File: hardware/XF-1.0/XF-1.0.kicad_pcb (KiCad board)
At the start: 2 copper layers, 121.3 x 99.7 mm, 16 parts

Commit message: modified:   Ferrite Transformer Calculation.xlsx 	modified:   README.md 	deleted:    hardware/XF-1.0/XF-1.0-backups/XF-1.0-2025-07-15_095716.zip 	new file:   hardware/XF-1.0/XF-1.0-backups/XF-1.0-2025-07-15_145509.zip 	new file:   hardware/XF-1.0/XF-1.0-backups/XF-1.0-2025-07-15_150114.zip 	new file:   hardware/XF-1.0/XF-1.0-backups/XF-1.0-2025-07-15_150614.zip 	new file:   hardware/XF-1.0/XF-1.0-backups/XF-1.0-2025-07-15_151503.zip 	new file:   hardware/XF-1.0/XF-1.0-backups/XF-1.0-2025-07-15_152320.zip 	new file:   hardware/XF-1.0/XF-1.0-backups/XF-1.0-2025-07-15_154638.zip 	modified:   hardware/XF-1.0/XF-1.0.kicad_pcb 	modified:   hardware/XF-1.0/XF-1.0.kicad_prl 	modified:   hardware/XF-1.0/XF-1.0.kicad_pro 	modified:   hardware/XF-1.0/XF-1.0.kicad_sch 	modified:   hardware/XF-1.0/_autosave-XF-1.0.kicad_sch 	modified:   hardware/XF-1.0/fp-info-cache
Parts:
- removed C1-1, C1-2, C1-3, C4-1, C4-2, C4-3: 1nF, Capacitor_THT:C_Rect_L13.0mm_W8.0mm_P10.00mm_FKS3_FKP3_MKS4
- removed C5, C6: 4.7nF, Capacitor_THT:C_Rect_L13.0mm_W8.0mm_P10.00mm_FKS3_FKP3_MKS4
- removed L3, L4: ~, Transformer_THT:Inductor-EE25
- removed TF1, TF2: ~, Transformer_THT:EE35-1P-1S-Vertical-2143
- added C1: 2.7nF, Capacitor_THT:C_Rect_L13.0mm_W8.0mm_P10.00mm_FKS3_FKP3_MKS4, F.Cu at (43.3, 124.5)
- added CN1: Conn_01x02, Connector_Molex:Molex_KK-396_5273-03A_1x03_P3.96mm_Vertical_2, F.Cu at (52.2, 52.5)
- added CN2: Conn_01x02, Connector_Molex:Molex_KK-396_5273-03A_1x03_P3.96mm_Vertical_2, F.Cu at (44.3, 139.9)
- added H1: ~, MountingHole:MountingHole_3mm_Pad, F.Cu at (27.3, 52.1)
- added H2: ~, MountingHole:MountingHole_3mm_Pad, F.Cu at (69.2, 52.1)
- added H3: ~, MountingHole:MountingHole_3mm_Pad, F.Cu at (27.3, 140.3)
- added H4: ~, MountingHole:MountingHole_3mm_Pad, F.Cu at (69.2, 140.3)
- added XF1: ~, Transformer_THT:Transformer_Toroid_Horizontal_OD40_ID23_H15, F.Cu at (48.3, 82.5)
- L1, L2: value ~ -> 29µH; footprint Transformer_THT:Inductor-EE25 -> Inductor_THT:L_Radial_Multilayer_D8.0mm_P12.70mm
- moved C3 19.8 mm to (60.3, 131.5), turned to -90 degrees
- moved L1 14.9 mm to (33.0, 113.0), turned to -90 degrees
- moved L2 12.8 mm to (63.5, 113.0), turned to -90 degrees
- moved C2 6.76 mm to (36.2, 131.5), turned to -90 degrees
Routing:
- net Net-(C4-3-Pad2): track 45.7 -> 0.00 mm, vias 2 -> 0
- net Net-(C4-1-Pad1): track 35.2 -> 0.00 mm, vias 2 -> 0
- net Net-(L3-Pad1): track 18.7 -> 0.00 mm
- net Net-(C1-Pad2): track 45.7 -> 27.1 mm
- net Net-(L4-Pad1): track 16.5 -> 0.00 mm
- net Net-(L2-Pad1): track 16.5 -> 28.1 mm
- net Net-(CN1-Pin_1): track 0.00 -> 11.3 mm
- net Net-(CN1-Pin_2): track 0.00 -> 11.3 mm
- net Net-(L1-Pad1): track 18.7 -> 28.1 mm
- net Net-(CN2-Pin_2): track 2.62 -> 11.4 mm
- net Net-(CN2-Pin_1): track 2.62 -> 11.4 mm
- net Net-(C4-2-Pad2): track 8.42 -> 0.00 mm, vias 2 -> 0
- net Net-(C1-2-Pad2): track 8.41 -> 0.00 mm, vias 2 -> 0
- net Net-(C1-1-Pad2): track 8.41 -> 0.00 mm, vias 2 -> 0
- net Net-(C4-1-Pad2): track 8.41 -> 0.00 mm, vias 2 -> 0
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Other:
- board size 121.3 x 99.7 mm -> 49.5 x 99.7 mm

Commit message: modified:   Ferrite Transformer Calculation.xlsx 	modified:   README.md 	deleted:    hardware/CTL-1.0/CTL-1.0-backups/CTL-1.0-2025-05-28_203223.zip 	new file:   hardware/CTL-1.0/CTL-1.0-backups/CTL-1.0-2025-07-16_143147.zip 	deleted:    hardware/PS-2.0/PS-2.0-backups/PS-2.0-2025-05-06_105341.zip 	new file:   hardware/PS-2.0/PS-2.0-backups/PS-2.0-2025-07-17_090338.zip 	deleted:    hardware/XF-1.0/#auto_saved_files# 	deleted:    hardware/XF-1.0/XF-1.0-backups/XF-1.0-2025-07-15_145509.zip 	new file:   hardware/XF-1.0/XF-1.0-backups/XF-1.0-2025-07-16_140719.zip 	new file:   hardware/XF-1.0/XF-1.0-backups/XF-1.0-2025-07-17_091914.zip 	new file:   hardware/XF-1.0/XF-1.0-backups/XF-1.0-2025-07-17_092825.zip 	new file:   hardware/XF-1.0/XF-1.0-backups/XF-1.0-2025-07-17_093426.zip 	new file:   hardware/XF-1.0/XF-1.0-backups/XF-1.0-2025-07-17_103845.zip 	new file:   hardware/XF-1.0/XF-1.0-backups/XF-1.0-2025-07-17_105026.zip 	new file:   hardware/XF-1.0/XF-1.0-backups/XF-1.0-2025-07-17_105651.zip 	modified:   hardware/XF-1.0/XF-1.0.kicad_pcb 	modified:   hardware/XF-1.0/XF-1.0.kicad_pro 	modified:   hardware/XF-1.0/XF-1.0.kicad_sch 	deleted:    hardware/XF-1.0/_autosave-XF-1.0.kicad_sch 	modified:   hardware/XF-1.0/fp-info-cache 	modified:   log.md
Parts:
- added C1-1: 2.7nF, Capacitor_THT:C_Rect_L13.0mm_W8.0mm_P10.00mm_FKS3_FKP3_MKS4, F.Cu at (30.6, 121.9)
- added C1-3: 2.7nF, Capacitor_THT:C_Rect_L13.0mm_W8.0mm_P10.00mm_FKS3_FKP3_MKS4, F.Cu at (66.1, 121.9)
- added C4-1: 2.7nF, Capacitor_THT:C_Rect_L13.0mm_W8.0mm_P10.00mm_FKS3_FKP3_MKS4, F.Cu at (87.7, 121.9)
- added C4-2: 2.7nF, Capacitor_THT:C_Rect_L13.0mm_W8.0mm_P10.00mm_FKS3_FKP3_MKS4, F.Cu at (105.5, 121.9)
- added C4-3: 2.7nF, Capacitor_THT:C_Rect_L13.0mm_W8.0mm_P10.00mm_FKS3_FKP3_MKS4, F.Cu at (123.3, 121.9)
- added C5: 4.7nF, Capacitor_THT:C_Rect_L13.0mm_W8.0mm_P10.00mm_FKS3_FKP3_MKS4, F.Cu at (87.7, 131.4)
- added C6: 4.7nF, Capacitor_THT:C_Rect_L13.0mm_W8.0mm_P10.00mm_FKS3_FKP3_MKS4, F.Cu at (133.3, 131.4)
- added CN3: Conn_01x02, Connector_Molex:Molex_KK-396_5273-03A_1x03_P3.96mm_Vertical_2, F.Cu at (93.8, 51.8)
- added CN4: Conn_01x02, Connector_Molex:Molex_KK-396_5273-03A_1x03_P3.96mm_Vertical_2, F.Cu at (106.5, 139.9)
- added L3: 29µH, Inductor_THT:L_Radial_Multilayer_D8.0mm_P12.70mm, F.Cu at (92.7, 106.7)
- added L4: 29µH, Inductor_THT:L_Radial_Multilayer_D8.0mm_P12.70mm, F.Cu at (128.3, 106.7)
- added XF2: ~, Transformer_THT:Transformer_Toroid_Horizontal_OD40_ID23_H15, F.Cu at (110.5, 78.7)
- moved H2 67.3 mm to (136.5, 50.2)
- moved H4 67.3 mm to (136.5, 142.2)
- moved CN1 25.7 mm to (78.0, 51.8)
- moved C3 15.8 mm to (76.1, 131.4), turned to 180 degrees
- moved L2 9.92 mm to (71.1, 106.7)
- moved L1 6.84 mm to (35.6, 106.7)
- moved XF1 6.35 mm to (53.3, 78.7)
- moved C1-2 5.68 mm to (48.3, 121.9)
- moved C2 5.64 mm to (30.6, 131.4), turned to 0 degrees
- moved CN2 5.08 mm to (49.4, 139.9)
- moved H1 1.91 mm to (27.3, 50.2)
- moved H3 1.91 mm to (27.3, 142.2)
- renumbered C1 to C1-2
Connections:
- C1-2 pad 1: Net-(C1-Pad1) -> Net-(C1-1-Pad2)
- C1-2 pad 2: Net-(C1-Pad2) -> Net-(C1-2-Pad2)
- C2 pad 1: Net-(C1-Pad1) -> Net-(C1-1-Pad1)
- C3 pad 1: Net-(C1-Pad2) -> Net-(C1-3-Pad2)
- L1 pad 2: Net-(C1-Pad1) -> Net-(C1-1-Pad1)
- L2 pad 2: Net-(C1-Pad2) -> Net-(C1-3-Pad2)
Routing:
- net Net-(C1-Pad2): track 27.1 -> 0.00 mm, vias 2 -> 0
- net Net-(C1-Pad1): track 27.1 -> 0.00 mm, vias 2 -> 0
- net Net-(CN3-Pin_1): track 0.00 -> 27.0 mm
- net Net-(C1-1-Pad1): track 0.00 -> 25.3 mm, vias 0 -> 2
- net Net-(C4-1-Pad1): track 0.00 -> 25.3 mm, vias 0 -> 2
- net Net-(C1-3-Pad2): track 0.00 -> 25.3 mm, vias 0 -> 2
- net Net-(C4-3-Pad2): track 0.00 -> 25.3 mm, vias 0 -> 2
- net Net-(L4-Pad1): track 0.00 -> 24.5 mm
- net Net-(L3-Pad1): track 0.00 -> 24.5 mm
- net Net-(CN3-Pin_2): track 0.00 -> 22.2 mm
- net Net-(CN4-Pin_1): track 0.00 -> 15.9 mm, vias 0 -> 1
- net Net-(CN4-Pin_2): track 0.00 -> 15.9 mm, vias 0 -> 1
- net Net-(CN1-Pin_2): track 11.3 -> 27.0 mm
- net Net-(CN1-Pin_1): track 11.3 -> 22.2 mm
- net Net-(C4-2-Pad2): track 0.00 -> 7.78 mm, vias 0 -> 2
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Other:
- board size 49.5 x 99.7 mm -> 116.8 x 99.7 mm

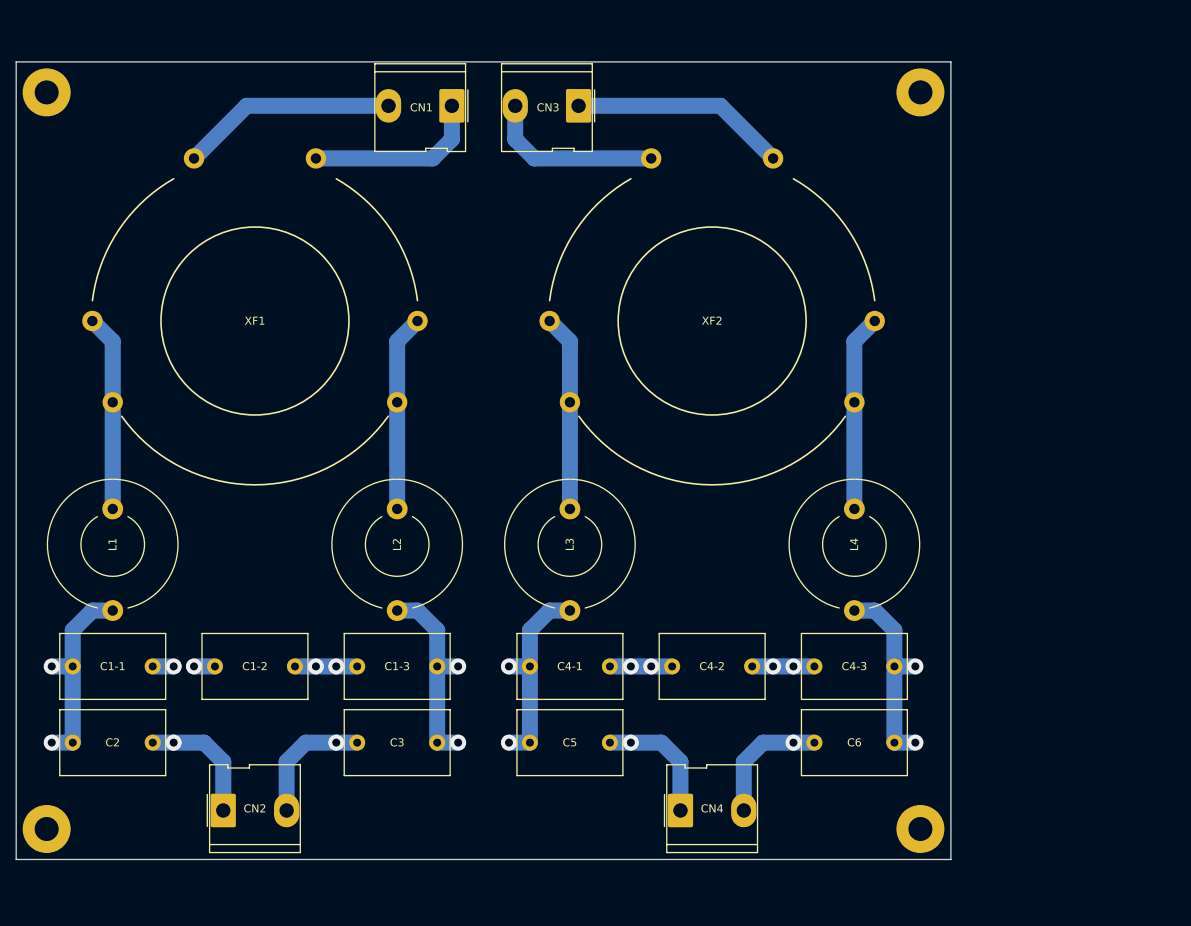
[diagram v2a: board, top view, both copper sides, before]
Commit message: deleted:    hardware/PS-2.0/PS-2.0-backups/PS-2.0-2025-05-06_110321.zip 	deleted:    hardware/PS-2.0/PS-2.0-backups/PS-2.0-2025-05-06_111001.zip 	deleted:    hardware/PS-2.0/PS-2.0-backups/PS-2.0-2025-05-06_111519.zip 	deleted:    hardware/PS-2.0/PS-2.0-backups/PS-2.0-2025-05-06_112237.zip 	new file:   hardware/PS-2.0/PS-2.0-backups/PS-2.0-2025-07-17_141237.zip 	new file:   hardware/PS-2.0/PS-2.0-backups/PS-2.0-2025-07-17_142153.zip 	new file:   hardware/PS-2.0/PS-2.0-backups/PS-2.0-2025-07-17_143639.zip 	new file:   hardware/PS-2.0/PS-2.0-backups/PS-2.0-2025-07-17_144647.zip 	deleted:    hardware/XF-1.0/XF-1.0-backups/XF-1.0-2025-07-17_091914.zip 	deleted:    hardware/XF-1.0/XF-1.0-backups/XF-1.0-2025-07-17_092825.zip 	deleted:    hardware/XF-1.0/XF-1.0-backups/XF-1.0-2025-07-17_093426.zip 	deleted:    hardware/XF-1.0/XF-1.0-backups/XF-1.0-2025-07-17_103845.zip 	deleted:    hardware/XF-1.0/XF-1.0-backups/XF-1.0-2025-07-17_105026.zip 	deleted:    hardware/XF-1.0/XF-1.0-backups/XF-1.0-2025-07-17_105651.zip 	new file:   hardware/XF-1.0/XF-1.0-backups/XF-1.0-2025-07-17_144932.zip 	new file:   hardware/XF-1.0/XF-1.0-backups/XF-1.0-2025-07-17_145542.zip 	new file:   hardware/XF-1.0/XF-1.0-backups/XF-1.0-2025-07-17_150101.zip 	new file:   hardware/XF-1.0/XF-1.0-backups/XF-1.0-2025-07-17_150621.zip 	new file:   hardware/XF-1.0/XF-1.0-backups/XF-1.0-2025-07-17_151256.zip 	new file:   hardware/XF-1.0/XF-1.0-backups/XF-1.0-2025-07-17_151907.zip 	modified:   hardware/XF-1.0/XF-1.0.kicad_pcb 	modified:   hardware/XF-1.0/XF-1.0.kicad_pro 	modified:   hardware/XF-1.0/XF-1.0.kicad_sch
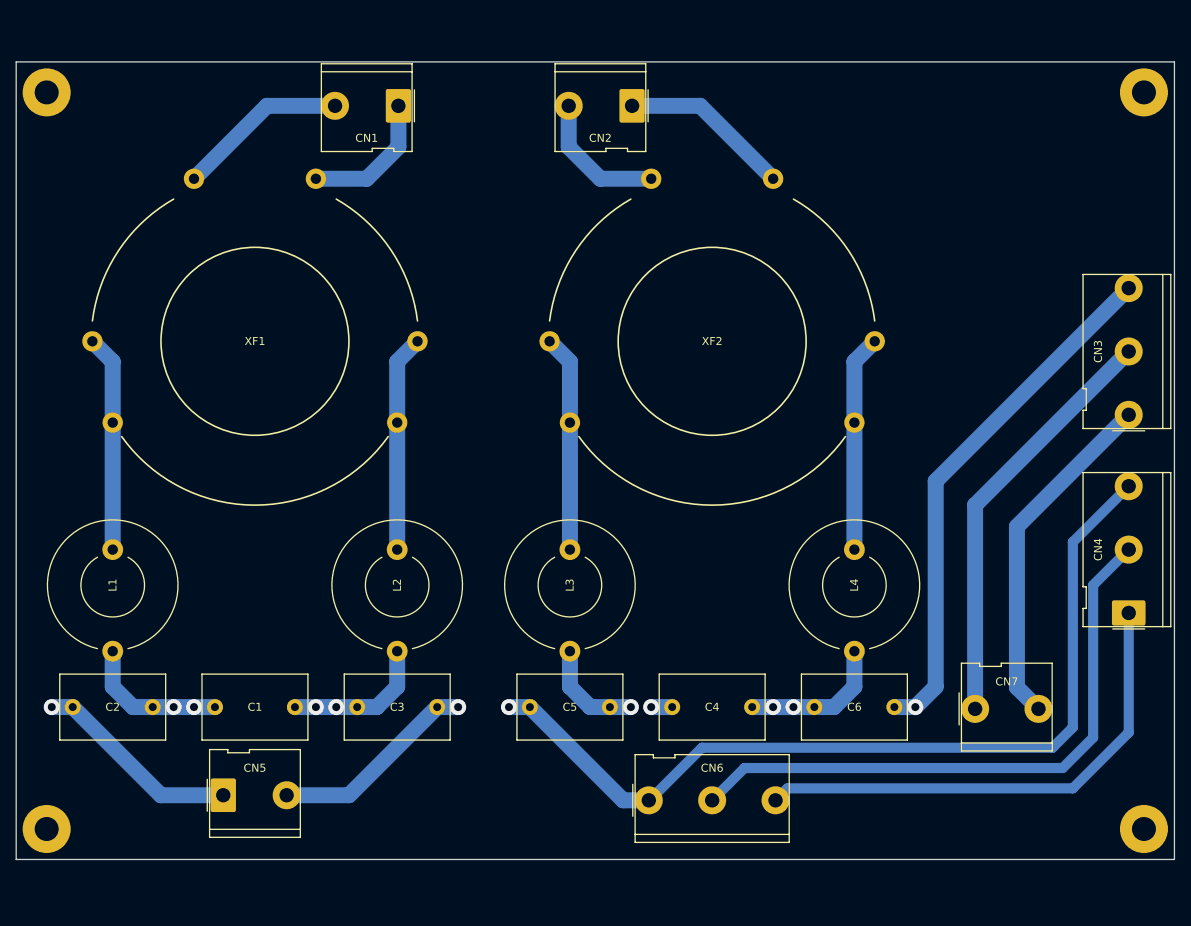
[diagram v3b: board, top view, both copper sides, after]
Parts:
- removed C1-1, C1-3, C4-1, C4-3: 2.7nF, Capacitor_THT:C_Rect_L13.0mm_W8.0mm_P10.00mm_FKS3_FKP3_MKS4
- added CN3: Conn_01x03, Connector_Molex:Molex_KK-396_5273-05A_1x05_P3.96mm_Vertical_2, F.Cu at (162.6, 90.5)
- added CN6: Conn_01x03, Connector_Molex:Molex_KK-396_5273-05A_1x05_P3.96mm_Vertical_2, F.Cu at (102.6, 138.7)
- added CN7: Conn_01x02, Connector_Molex:Molex_KK-396_5273-03A_1x03_P3.96mm_Vertical_2, F.Cu at (143.4, 127.2)
- CN4: value Conn_01x02 -> Conn_01x03; footprint Connector_Molex:Molex_KK-396_5273-03A_1x03_P3.96mm_Vertical_2 -> Connector_Molex:Molex_KK-396_5273-05A_1x05_P3.96mm_Vertical_2
- moved CN4 61.2 mm to (162.6, 115.2), turned to 90 degrees
- moved H2 27.9 mm to (164.5, 50.2)
- moved H4 27.9 mm to (164.5, 142.2)
- moved C6 10.9 mm to (123.3, 127.0), turned to 0 degrees
- moved C2 10.9 mm to (40.6, 127.0), turned to 180 degrees
- moved C3 10.9 mm to (66.1, 127.0), turned to 0 degrees
- moved C5 10.9 mm to (97.7, 127.0), turned to 180 degrees
- moved CN1 6.69 mm to (71.3, 51.8)
- moved CN2 6.69 mm to (100.5, 51.8)
- moved C1 5.08 mm to (48.3, 127.0)
- moved C4 5.08 mm to (105.5, 127.0)
- moved L1 5.08 mm to (35.6, 111.8)
- moved L2 5.08 mm to (71.1, 111.8)
- moved L3 5.08 mm to (92.7, 111.8)
- moved L4 5.08 mm to (128.3, 111.8)
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- renumbered C1-2 to C1, C4-2 to C4, CN3 to CN2, CN2 to CN5
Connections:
- C1 pad 1: Net-(C1-1-Pad2) -> Net-(C1-Pad1)
- C1 pad 2: Net-(C1-2-Pad2) -> Net-(C1-Pad2)
- C2 pad 1: Net-(C1-1-Pad1) -> Net-(C1-Pad1)
- C3 pad 1: Net-(C1-3-Pad2) -> Net-(C1-Pad2)
- C4 pad 1: Net-(C4-1-Pad2) -> Net-(C4-Pad1)
- C4 pad 2: Net-(C4-2-Pad2) -> Net-(C4-Pad2)
- C5 pad 1: Net-(C4-1-Pad1) -> Net-(C4-Pad1)
- C5 pad 2: Net-(CN4-Pin_1) -> Net-(CN4-Pin_3)
- C6 pad 1: Net-(C4-3-Pad2) -> Net-(C4-Pad2)
- C6 pad 2: Net-(CN4-Pin_2) -> Net-(CN3-Pin_3)
- L1 pad 2: Net-(C1-1-Pad1) -> Net-(C1-Pad1)
- L2 pad 2: Net-(C1-3-Pad2) -> Net-(C1-Pad2)
- L3 pad 2: Net-(C4-1-Pad1) -> Net-(C4-Pad1)
- L4 pad 2: Net-(C4-3-Pad2) -> Net-(C4-Pad2)
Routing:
- net Net-(CN4-Pin_3): track 0.00 -> 112.1 mm, vias 0 -> 1
- net Net-(CN3-Pin_3): track 0.00 -> 66.0 mm, vias 0 -> 1
- net Net-(CN4-Pin_2): track 15.9 -> 76.2 mm, vias 1 -> 0
- net Net-(CN3-Pin_2): track 0.00 -> 52.6 mm
- net Net-(CN4-Pin_1): track 15.9 -> 62.6 mm, vias 1 -> 0
- net Net-(CN3-Pin_1): track 0.00 -> 43.7 mm
- net Net-(C1-1-Pad1): track 25.3 -> 0.00 mm, vias 2 -> 0
- net Net-(C4-1-Pad1): track 25.3 -> 0.00 mm, vias 2 -> 0
- net Net-(C1-3-Pad2): track 25.3 -> 0.00 mm, vias 2 -> 0
- net Net-(C4-3-Pad2): track 25.3 -> 0.00 mm, vias 2 -> 0
- net Net-(C4-Pad2): track 0.00 -> 18.3 mm, vias 0 -> 2
- net Net-(C1-Pad1): track 0.00 -> 18.3 mm, vias 0 -> 2
- net Net-(C1-Pad2): track 0.00 -> 18.3 mm, vias 0 -> 2
- net Net-(C4-Pad1): track 0.00 -> 15.7 mm, vias 0 -> 2
- net Net-(CN5-Pin_1): track 15.9 -> 26.0 mm
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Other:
- board size 116.8 x 99.7 mm -> 144.8 x 99.7 mm

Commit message: modified:   README.md 	deleted:    hardware/CTL-1.0/CTL-1.0-backups/CTL-1.0-2025-05-28_203806.zip 	deleted:    hardware/CTL-1.0/CTL-1.0-backups/CTL-1.0-2025-05-28_204313.zip 	deleted:    hardware/CTL-1.0/CTL-1.0-backups/CTL-1.0-2025-05-30_173028.zip 	deleted:    hardware/CTL-1.0/CTL-1.0-backups/CTL-1.0-2025-05-30_174116.zip 	deleted:    hardware/CTL-1.0/CTL-1.0-backups/CTL-1.0-2025-05-30_175122.zip 	new file:   hardware/CTL-1.0/CTL-1.0-backups/CTL-1.0-2025-07-24_151142.zip 	new file:   hardware/CTL-1.0/CTL-1.0-backups/CTL-1.0-2025-07-24_172002.zip 	new file:   hardware/CTL-1.0/CTL-1.0-backups/CTL-1.0-2025-07-25_175122.zip 	new file:   hardware/CTL-1.0/CTL-1.0-backups/CTL-1.0-2025-07-26_120011.zip 	new file:   hardware/CTL-1.0/CTL-1.0-backups/CTL-1.0-2025-07-26_120808.zip 	modified:   hardware/CTL-1.0/CTL-1.0.kicad_pcb 	modified:   hardware/CTL-1.0/CTL-1.0.kicad_pro 	new file:   hardware/CTL-1.0/CTL-1.0.step 	deleted:    hardware/MSD-1.0/MSD-1.0-backups/MSD-1.0-2025-04-11_111943.zip 	deleted:    hardware/MSD-1.0/MSD-1.0-backups/MSD-1.0-2025-04-11_113401.zip 	new file:   hardware/MSD-1.0/MSD-1.0-backups/MSD-1.0-2025-07-25_163151.zip 	new file:   hardware/MSD-1.0/MSD-1.0-backups/MSD-1.0-2025-07-25_171843.zip 	modified:   hardware/MSD-1.0/MSD-1.0.kicad_pcb 	modified:   hardware/MSD-1.0/MSD-1.0.step 	new file:   hardware/MSD-1.1/MSD-1.1-backups/MSD-1.1-2025-07-24_151252.zip 	new file:   hardware/MSD-1.1/MSD-1.1-backups/MSD-1.1-2025-07-25_152939.zip 	new file:   hardware/MSD-1.1/MSD-1.1-backups/MSD-1.1-2025-07-25_162346.zip 	new file:   hardware/MSD-1.1/MSD-1.1-backups/MSD-1.1-2025-07-25_162917.zip 	modified:   hardware/MSD-1.1/MSD-1.1.kicad_pcb 	modified:   hardware/MSD-1.1/MSD-1.1.step 	modified:   hardware/MSD-1.1/fp-info-cache 	new file:   hardware/MSD-2.0/MSD-2.0-backups/MSD-2.0-2025-07-24_151230.zip 	deleted:    hardware/PS-2.0/PS-2.0-backups/PS-2.0-2025-05-07_010425.zip 	deleted:    hardware/PS-2.0/PS-2.0-backups/PS-2.0-2025-05-09_084820.zip 	deleted:    hardware/P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
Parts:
- removed the H2 at (164.5, 50.2)
- added H3: ~, MountingHole:MountingHole_3mm_Pad, F.Cu at (110.8, 141.3)
- moved CN7 112.7 mm to (30.9, 120.5), turned to -90 degrees
- moved H4 105.2 mm to (110.8, 51.8)
- moved CN6 87.4 mm to (30.9, 88.6), turned to -90 degrees
- moved C6 80.7 mm to (43.2, 137.2), turned to -90 degrees
- moved CN2 79.1 mm to (120.2, 128.4), turned to 90 degrees
- moved CN5 75.7 mm to (30.9, 64.6), turned to -90 degrees
- moved L4 72.9 mm to (59.1, 134.6), turned to 180 degrees
- moved C2 71.2 mm to (43.2, 55.8), turned to 90 degrees
- moved C1 63.6 mm to (43.2, 63.6), turned to -90 degrees
- moved C4 62.8 mm to (43.2, 119.5), turned to -90 degrees
- moved L1 58.3 mm to (59.1, 58.4), turned to 180 degrees
- moved C5 56.6 mm to (43.2, 111.7), turned to 90 degrees
- moved CN1 53.2 mm to (120.2, 72.5), turned to 90 degrees
- moved C3 51.1 mm to (43.2, 81.4), turned to -90 degrees
- moved CN3 49.0 mm to (120.2, 115.2)
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- renumbered H3 to H2
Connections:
- C6 pad 2: Net-(CN3-Pin_3) -> Net-(CN3-Pin_1)
- CN7 pad 1: Net-(CN3-Pin_2) -> Net-(CN3-Pin_3)
- CN7 pad 2: Net-(CN3-Pin_1) -> Net-(CN3-Pin_2)
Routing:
- net Net-(CN3-Pin_1): track 43.7 -> 112.9 mm, vias 0 -> 1
- net Net-(CN3-Pin_2): track 52.6 -> 98.1 mm
- net Net-(CN3-Pin_3): track 66.0 -> 100.3 mm, vias 1 -> 0
- net Net-(CN4-Pin_1): track 62.6 -> 96.7 mm
- net Net-(CN4-Pin_2): track 76.2 -> 101.2 mm
- net Net-(CN1-Pin_2): track 21.4 -> 11.3 mm
- net Net-(CN2-Pin_1): track 21.4 -> 11.3 mm
- net Net-(CN4-Pin_3): track 112.1 -> 105.1 mm
- net Net-(CN2-Pin_2): track 17.1 -> 11.3 mm
- net Net-(CN1-Pin_1): track 17.1 -> 11.3 mm
- net Net-(L3-Pad1): track 27.1 -> 31.1 mm
- net Net-(L2-Pad1): track 27.1 -> 31.1 mm
- net Net-(L4-Pad1): track 27.1 -> 31.1 mm
- net Net-(L1-Pad1): track 27.1 -> 31.1 mm
- net Net-(C4-Pad2): track 18.3 -> 15.4 mm
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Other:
- board size 144.8 x 99.7 mm -> 100.3 x 111.8 mm
